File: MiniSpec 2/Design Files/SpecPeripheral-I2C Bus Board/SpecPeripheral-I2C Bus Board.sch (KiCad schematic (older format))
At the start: 8 parts, among them IC1 TCA9548APWR, J1 SSM-104-F-DV, J2 SSM-104-F-DV, J3 SSM-104-F-DV, J4 SSM-104-F-DV, J5 M20-7910442R

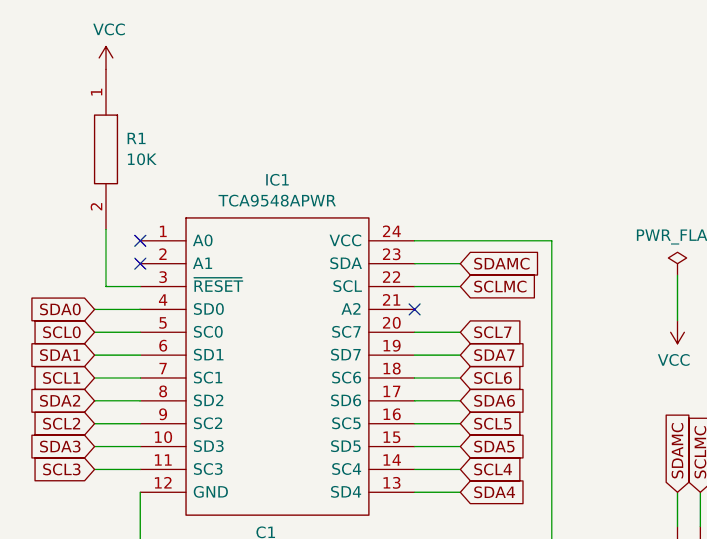
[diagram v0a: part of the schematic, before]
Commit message: Finished I2C Bus Board, added raw data of spec readings
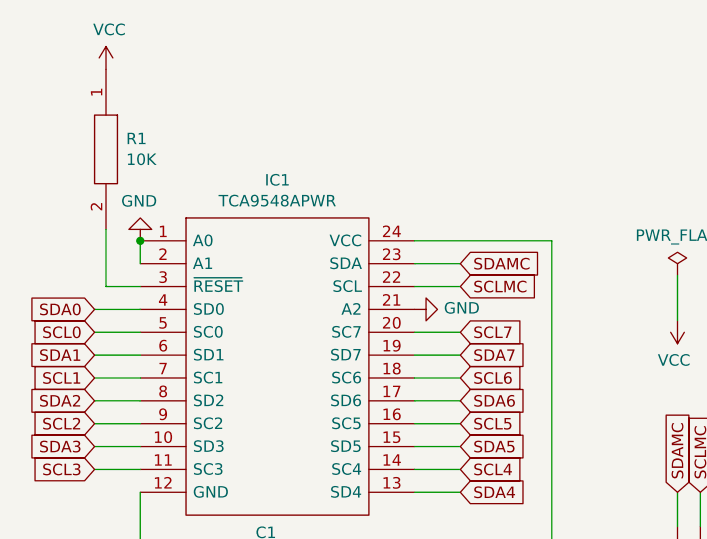
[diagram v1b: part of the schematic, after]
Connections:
- net GND: now also IC1.1 (A0), IC1.2 (A1), IC1.21 (A2)
- no-connect marks 3 -> 0
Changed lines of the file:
@@
 Wire Wire Line
 	4000 2950 3800 2950
-NoConn ~ 2600 1850
-NoConn ~ 2600 1950
-NoConn ~ 3800 2150
 Wire Wire Line
 	2450 2050 2600 2050
@@
 	0    1    1    0
 $EndComp
+$Comp
+L power:GND #PWR?
+U 1 1 5F612DB1
+P 2600 1850
+F 0 "#PWR?" H 2600 1600 50  0001 C CNN
+F 1 "GND" H 2605 1677 50  0000 C CNN
+F 2 "" H 2600 1850 50  0001 C CNN
+F 3 "" H 2600 1850 50  0001 C CNN
+	1    2600 1850
+	-1   0    0    1
+$EndComp
+Wire Wire Line
+	2600 1950 2600 1850
+Connection ~ 2600 1850
+$Comp
+L power:GND #PWR?
+U 1 1 5F615BFB
+P 3800 2150
+F 0 "#PWR?" H 3800 1900 50  0001 C CNN
+F 1 "GND" V 3805 2022 50  0000 R CNN
+F 2 "" H 3800 2150 50  0001 C CNN
+F 3 "" H 3800 2150 50  0001 C CNN
+	1    3800 2150
+	0    -1   -1   0
+$EndComp
 $EndSCHEMATC
